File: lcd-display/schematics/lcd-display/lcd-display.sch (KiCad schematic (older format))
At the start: 11 parts, among them U1 74LS00, U2 74LS04, U3 74LS245, U4 74LS32

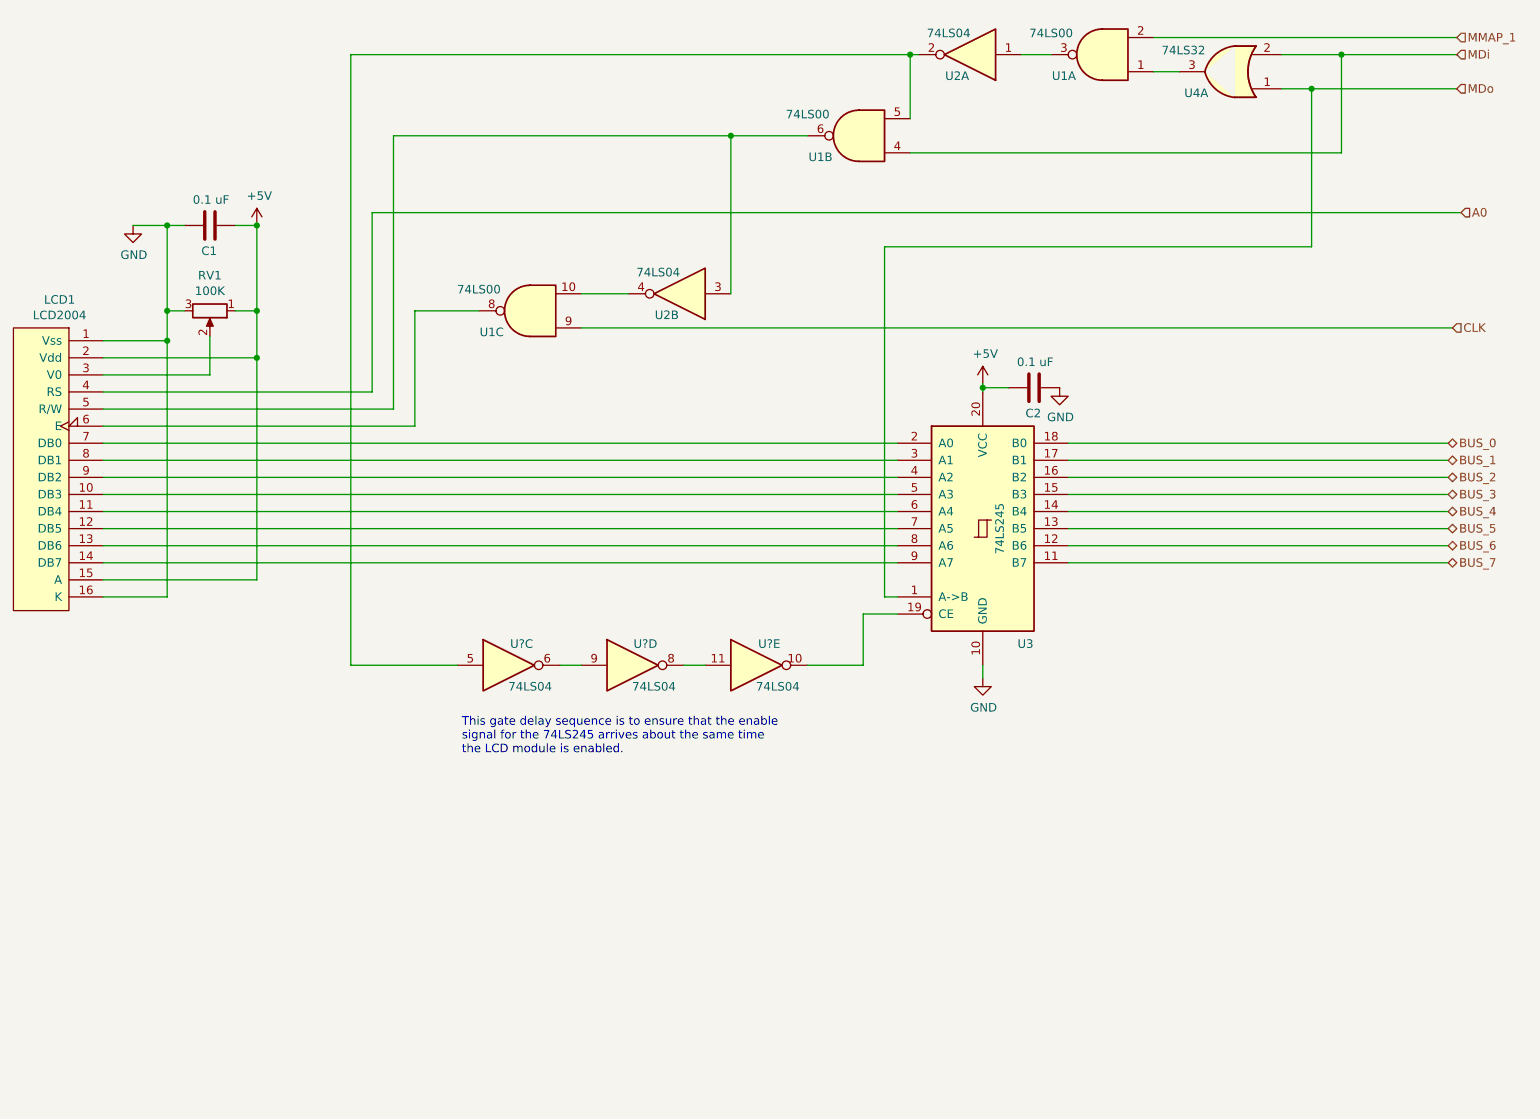
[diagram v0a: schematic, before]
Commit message: first working version of LCD module
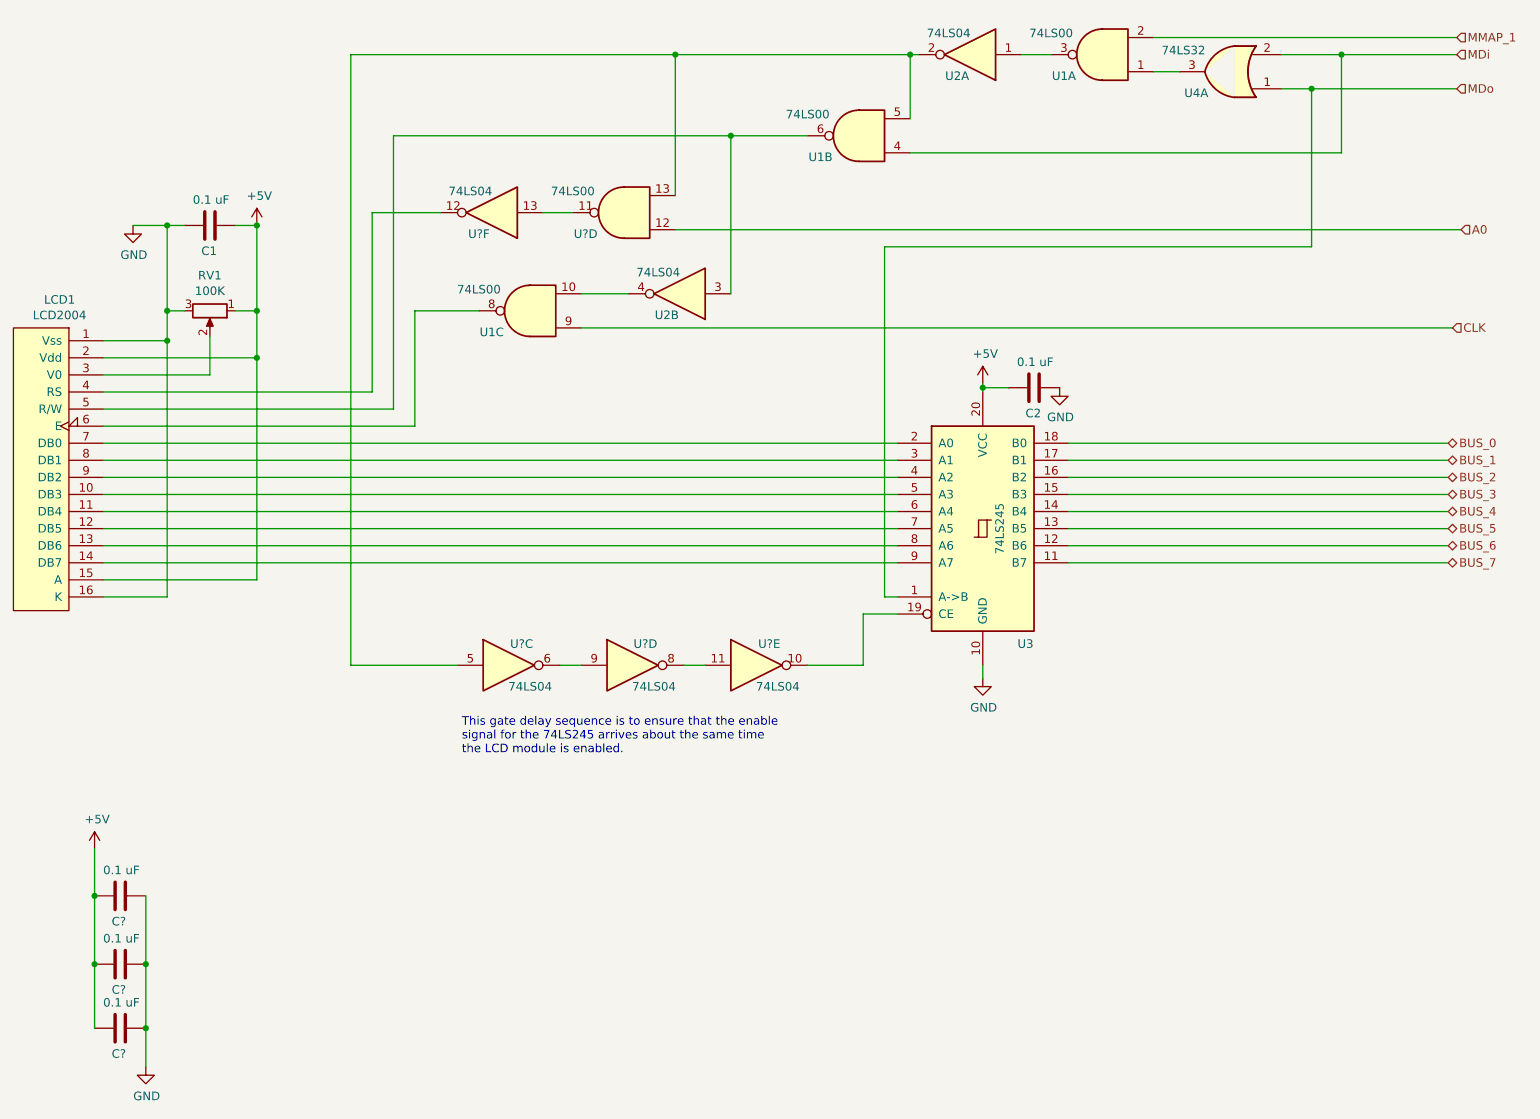
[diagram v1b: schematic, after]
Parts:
- added C? (x3): 0.1 uF, symbol Device:C
- added U?: 74LS00, symbol 74xx:74LS00
- added U?: 74LS04, symbol 74xx:74LS04
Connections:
- net +5V: now also C?.2, C?.2, C?.2
- net A0: now also U?.12; no longer LCD1.4 (RS)
- net GND: now also C?.1, C?.1, C?.1
- net at U1.5, U2.2, U?.5: now also U?.13
- new net: LCD1.4 (RS), U?.12
- new net: U?.11, U?.13
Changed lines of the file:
@@
 Wire Wire Line
 	9250 1475 6725 1475
-Text HLabel 9950 1825 2    50   Input ~ 0
+Text HLabel 9950 1925 2    50   Input ~ 0
 A0
 Text HLabel 9900 2500 2    50   Input ~ 0
@@
 $EndComp
 Wire Wire Line
-	8150 800  9925 800
-Wire Wire Line
 	5675 2300 5675 1375
 Connection ~ 5675 1375
@@
 Wire Wire Line
 	3825 2400 4200 2400
-Wire Wire Line
-	9950 1825 3575 1825
 Wire Wire Line
 	3575 1825 3575 2875
@@
 	4675 4475 4800 4475
 Wire Wire Line
-	6725 900  3450 900
+	6725 900  5350 900
 Wire Wire Line
 	3450 900  3450 4475
@@
 Text Notes 4100 5000 0    50   ~ 0
 This gate delay sequence is to ensure that the enable\nsignal for the 74LS245 arrives about the same time\nthe LCD module is enabled.
+$Comp
+L Device:C C?
+U 1 1 61D87343
+P 2100 5825
+F 0 "C?" V 2250 5775 50  0000 L CNN
+F 1 "0.1 uF" V 1950 5725 50  0000 L CNN
+F 2 "" H 2138 5675 50  0001 C CNN
+F 3 "~" H 2100 5825 50  0001 C CNN
+	1    2100 5825
+	0    1    1    0
+$EndComp
+$Comp
+L Device:C C?
+U 1 1 61D87A90
+P 2100 6225
+F 0 "C?" V 2250 6175 50  0000 L CNN
+F 1 "0.1 uF" V 1950 6125 50  0000 L CNN
+F 2 "" H 2138 6075 50  0001 C CNN
+F 3 "~" H 2100 6225 50  0001 C CNN
+	1    2100 6225
+	0    1    1    0
+$EndComp
+$Comp
+L Device:C C?
+U 1 1 61D8812F
+P 2100 6600
+F 0 "C?" V 2250 6550 50  0000 L CNN
+F 1 "0.1 uF" V 1950 6500 50  0000 L CNN
+F 2 "" H 2138 6450 50  0001 C CNN
+F 3 "~" H 2100 6600 50  0001 C CNN
+	1    2100 6600
+	0    1    1    0
+$EndComp
+Wire Wire Line
+	1950 6600 1950 6225
+Wire Wire Line
+	1950 6225 1950 5825
+Connection ~ 1950 6225
+Wire Wire Line
+	2250 5825 2250 6225
+Wire Wire Line
+	2250 6225 2250 6600
+Connection ~ 2250 6225
+$Comp
+L power:GND #PWR?
+U 1 1 61D90BAC
+P 2250 6825
+F 0 "#PWR?" H 2250 6575 50  0001 C CNN
+F 1 "GND" H 2255 6652 50  0000 C CNN
+F 2 "" H 2250 6825 50  0001 C CNN
+F 3 "" H 2250 6825 50  0001 C CNN
+	1    2250 6825
+	1    0    0    -1
+$EndComp
+$Comp
+L power:+5V #PWR?
+U 1 1 61D91162
+P 1950 5550
+F 0 "#PWR?" H 1950 5400 50  0001 C CNN
+F 1 "+5V" H 1965 5723 50  0000 C CNN
+F 2 "" H 1950 5550 50  0001 C CNN
+F 3 "" H 1950 5550 50  0001 C CNN
+	1    1950 5550
+	1    0    0    -1
+$EndComp
+Wire Wire Line
+	1950 5825 1950 5550
+Connection ~ 1950 5825
+Wire Wire Line
+	2250 6600 2250 6825
+Connection ~ 2250 6600
+$Comp
+L 74xx:74LS00 U?
+U 4 1 61CB2133
+P 5050 1825
+F 0 "U?" H 5275 1950 50  0000 C CNN
+F 1 "74LS00" H 5350 1700 50  0000 C CNN
+F 2 "" H 5050 1825 50  0001 C CNN
+F 3 "http://www.ti.com/lit/gpn/sn74ls00" H 5050 1825 50  0001 C CNN
+	4    5050 1825
+	-1   0    0    1
+$EndComp
+$Comp
+L 74xx:74LS04 U?
+U 6 1 61CBA352
+P 4275 1825
+F 0 "U?" H 4350 1950 50  0000 C CNN
+F 1 "74LS04" H 4400 1700 50  0000 C CNN
+F 2 "" H 4275 1825 50  0001 C CNN
+F 3 "http://www.ti.com/lit/gpn/sn74LS04" H 4275 1825 50  0001 C CNN
+	6    4275 1825
+	-1   0    0    1
+$EndComp
+Wire Wire Line
+	3575 1825 3975 1825
+Wire Wire Line
+	4575 1825 4750 1825
+Wire Wire Line
+	5350 1925 9950 1925
+Wire Wire Line
+	8150 800  9925 800
+Wire Wire Line
+	5350 1725 5350 900
+Connection ~ 5350 900
+Wire Wire Line
+	5350 900  3450 900
 $EndSCHEMATC

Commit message: improved handling of timming differences between clock and mmap
The MMAP_1 signal is noticablylater than the clock due to all the gates it has to go through in the memory map mananger. This caused issues with the trailing edge enable fo the LCD2004 module in that the inverted clock would go high moments before the MMAP_1 signal would go low. This in turn caused a spurious trailing edge event into the Enable input of the LCD2004 module, causing weirdness with the cursor.
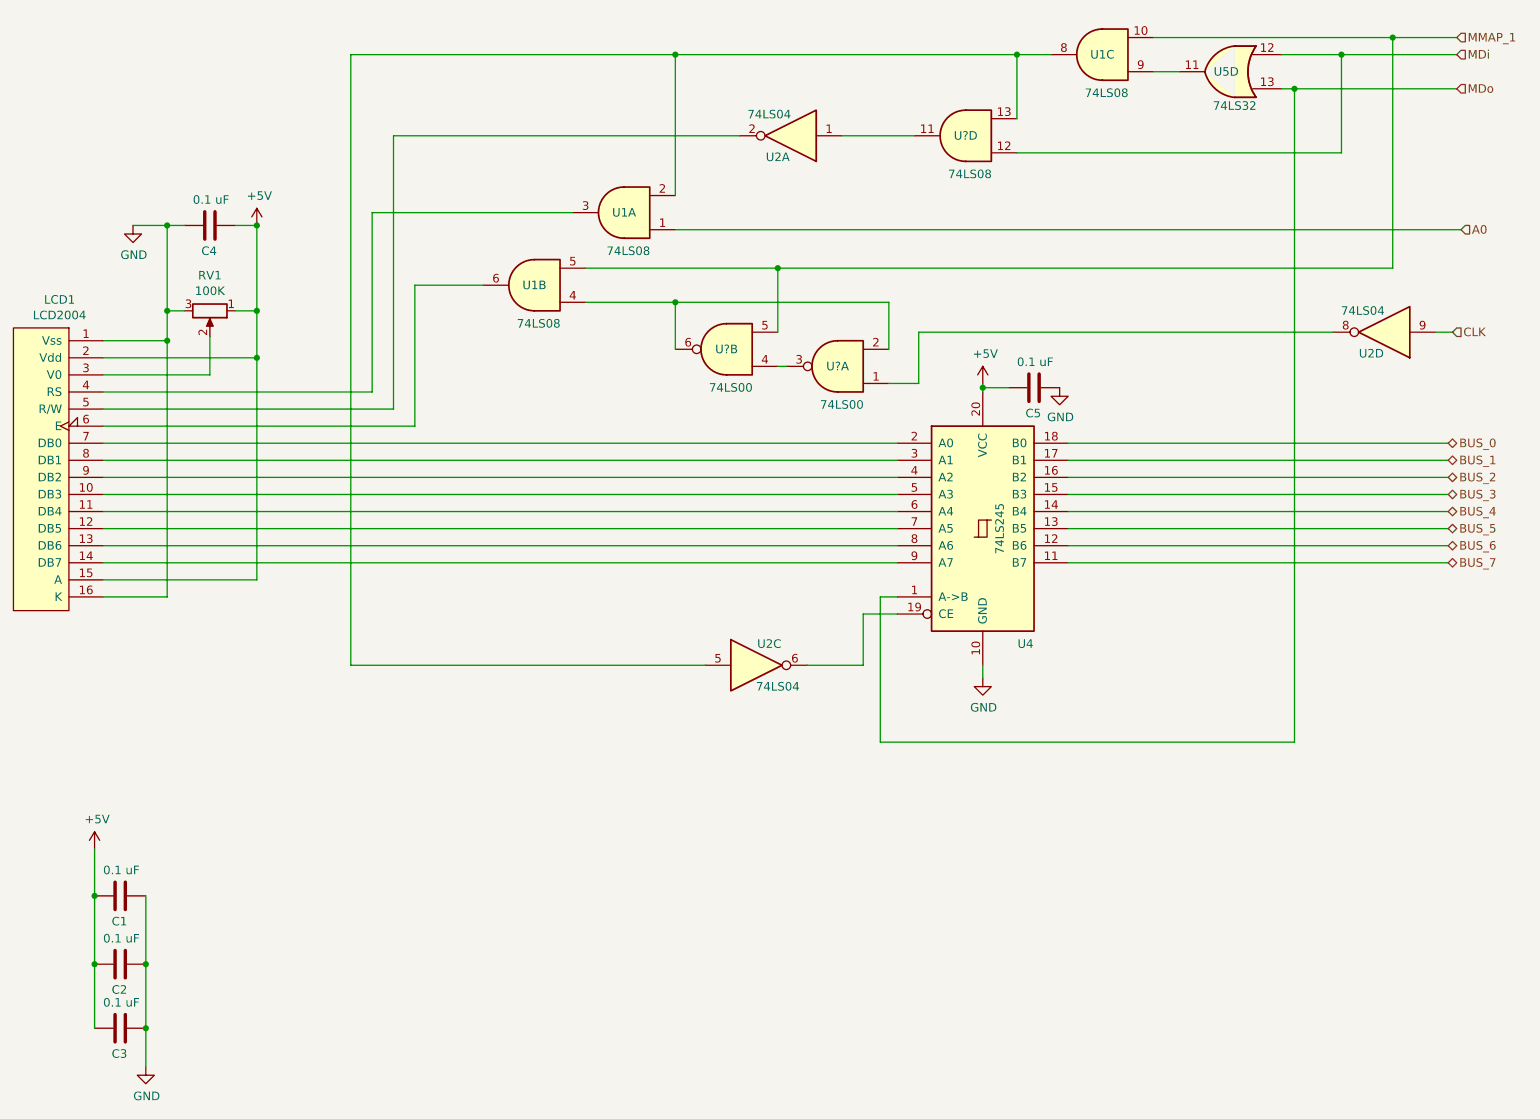
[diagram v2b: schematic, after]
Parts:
- removed U1, U?: 74LS00, symbol 74xx:74LS00
- removed U2, U?: 74LS04, symbol 74xx:74LS04
- added U1, U?: 74LS08, symbol 74xx:74LS08
- added U? (x2): 74LS00, symbol 74xx:74LS00
- gave numbers to parts that had none: 4
- renumbered C1 to C4, C2 to C5, U3 to U4, U4 to U5
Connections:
- net A0: now also U1.1
- net CLK: now also U2.9
- net MDi: now also U5.12, U?.12; no longer U5.2
- net MDo: now also U5.13; no longer U5.1
- net MMAP_1: now also U1.10, U1.5, U?.5
- net at LCD1.4 (RS): now also U1.3
- net at LCD1.5 (R/W): now also U2.2
- net at LCD1.6 (E): now also U1.6
- net at U4.19 (CE): now also U2.6; no longer U2.10
- net at U2.8: now also U?.1; no longer U2.11
- new net: U1.9, U5.11
- new net: U1.2, U1.8, U2.5, U?.13
- new net: U1.4, U?.2, U?.6
- new net: U2.1, U?.11
- new net: U?.3, U?.4
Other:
- note removed: "This gate delay sequence is to ensure that the enable\nsignal for the 74LS245 arrives about the same time\nthe LCD module is enabled."
- moved on the sheet: U2D

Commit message: address stability issues caused by inductance
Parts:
- removed unit 2 of U1
- added C6: 1 pF, symbol Device:C
- added unit 3 of U1
- gave numbers to parts that had none: 2
- renumbered U1 to U2, U2 to U3
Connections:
- net GND: now also C6.2
- net MDi: now also C6.1
- net MMAP_1: no longer U1.5
- net at LCD1.6 (E): now also U1.8
- net at U2.11, U3.1: now also U1.5, U1.10
- net at U1.3, U1.4: now also U1.9
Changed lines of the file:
@@
 $EndComp
 Wire Wire Line
-	9925 900  9250 900
+	9925 900  9650 900
 Wire Wire Line
 	8300 1000 8150 1000
@@
 	2000 2775 2625 2775
 $Comp
-L 74xx:74LS04 U2
+L 74xx:74LS04 U3
 U 3 1 61D71BDF
 P 5825 4475
-F 0 "U2" H 5900 4600 50  0000 C CNN
+F 0 "U3" H 5900 4600 50  0000 C CNN
 F 1 "74LS04" H 5950 4350 50  0000 C CNN
 F 2 "" H 5825 4475 50  0001 C CNN
@@
 $EndComp
 $Comp
-L 74xx:74LS04 U2
+L 74xx:74LS04 U3
 U 4 1 61D73754
 P 9500 2525
-F 0 "U2" H 9575 2650 50  0000 C CNN
+F 0 "U3" H 9575 2650 50  0000 C CNN
 F 1 "74LS04" H 9625 2400 50  0000 C CNN
 F 2 "" H 9500 2525 50  0001 C CNN
@@
 $EndComp
 $Comp
-L 74xx:74LS04 U2
+L 74xx:74LS04 U3
 U 1 1 61D74674
 P 6025 1375
-F 0 "U2" H 6100 1500 50  0000 C CNN
+F 0 "U3" H 6100 1500 50  0000 C CNN
 F 1 "74LS04" H 6150 1250 50  0000 C CNN
 F 2 "" H 6025 1375 50  0001 C CNN
@@
 	5350 1925 9950 1925
 Wire Wire Line
-	8150 800  9550 800
-Wire Wire Line
 	5350 1725 5350 900
 Connection ~ 5350 900
@@
 	5350 900  3450 900
 $Comp
-L 74xx:74LS08 U1
+L 74xx:74LS08 U2
 U 3 1 61D13CBF
 P 7850 900
-F 0 "U1" H 7850 900 50  0000 C CNN
+F 0 "U2" H 7850 900 50  0000 C CNN
 F 1 "74LS08" H 7825 1125 50  0000 C CNN
 F 2 "" H 7850 900 50  0001 C CNN
@@
 	7350 900  7550 900
 $Comp
-L 74xx:74LS08 U1
+L 74xx:74LS08 U2
 U 1 1 61D21297
 P 5050 1825
-F 0 "U1" H 5050 1825 50  0000 C CNN
+F 0 "U2" H 5050 1825 50  0000 C CNN
 F 1 "74LS08" H 5025 2050 50  0000 C CNN
 F 2 "" H 5050 1825 50  0001 C CNN
@@
 Wire Wire Line
 	3700 1375 5725 1375
-$Comp
-L 74xx:74LS08 U1
-U 2 1 61D5EE45
-P 4525 2250
-F 0 "U1" H 4525 2250 50  0000 C CNN
-F 1 "74LS08" H 4500 2475 50  0000 C CNN
-F 2 "" H 4525 2250 50  0001 C CNN
-F 3 "http://www.ti.com/lit/gpn/sn74LS08" H 4525 2250 50  0001 C CNN
-	2    4525 2250
-	-1   0    0    1
-$EndComp
 Wire Wire Line
 	3450 4475 5525 4475
@@
 	3825 2250 3825 3075
 $Comp
-L 74xx:74LS08 U?
+L 74xx:74LS08 U2
 U 4 1 61DA5054
 P 7050 1375
-F 0 "U?" H 7050 1375 50  0000 C CNN
+F 0 "U2" H 7050 1375 50  0000 C CNN
 F 1 "74LS08" H 7025 1600 50  0000 C CNN
 F 2 "" H 7050 1375 50  0001 C CNN
@@
 	9800 2525 9900 2525
 $Comp
-L 74xx:74LS00 U?
+L 74xx:74LS00 U1
 U 1 1 61DBB399
 P 6300 2725
-F 0 "U?" H 6300 2725 50  0000 C CNN
+F 0 "U1" H 6300 2725 50  0000 C CNN
 F 1 "74LS00" H 6275 2950 50  0000 C CNN
 F 2 "" H 6300 2725 50  0001 C CNN
@@
 $EndComp
 $Comp
-L 74xx:74LS00 U?
+L 74xx:74LS00 U1
 U 2 1 61DC0804
 P 5650 2625
-F 0 "U?" H 5650 2625 50  0000 C CNN
+F 0 "U1" H 5650 2625 50  0000 C CNN
 F 1 "74LS00" H 5625 2850 50  0000 C CNN
 F 2 "" H 5650 2625 50  0001 C CNN
@@
 $EndComp
 Wire Wire Line
-	4825 2350 5350 2350
-Wire Wire Line
 	6600 2350 6600 2625
 Wire Wire Line
@@
 Wire Wire Line
 	5350 2625 5350 2350
-Connection ~ 5350 2350
 Wire Wire Line
 	5350 2350 6600 2350
@@
 Wire Wire Line
 	5350 900  7350 900
+Wire Wire Line
+	6325 1375 6500 1375
+Wire Wire Line
+	8150 800  9925 800
+Wire Wire Line
+	5950 2150 6500 2150
+Wire Wire Line
+	6500 2150 6500 1375
 Connection ~ 5950 2150
-Wire Wire Line
-	6325 1375 6750 1375
-Wire Wire Line
-	9550 2150 9550 800
-Wire Wire Line
-	5950 2150 9550 2150
-Connection ~ 9550 800
-Wire Wire Line
-	9550 800  9925 800
+Connection ~ 6500 1375
+Wire Wire Line
+	6500 1375 6750 1375
+Wire Wire Line
+	6000 2725 6000 2975
+Wire Wire Line
+	6000 2975 4825 2975
+Wire Wire Line
+	4825 2975 4825 2350
+Connection ~ 6000 2725
+$Comp
+L 74xx:74LS00 U1
+U 3 1 61D07816
+P 4525 2250
+F 0 "U1" H 4525 2250 50  0000 C CNN
+F 1 "74LS00" H 4500 2475 50  0000 C CNN
+F 2 "" H 4525 2250 50  0001 C CNN
+F 3 "http://www.ti.com/lit/gpn/sn74ls00" H 4525 2250 50  0001 C CNN
+	3    4525 2250
+	-1   0    0    1
+$EndComp
+$Comp
+L Device:C C6
+U 1 1 61D0EEB6
+P 9650 1400
+F 0 "C6" H 9765 1446 50  0000 L CNN
+F 1 "1 pF" H 9765 1355 50  0000 L CNN
+F 2 "" H 9688 1250 50  0001 C CNN
+F 3 "~" H 9650 1400 50  0001 C CNN
+	1    9650 1400
+	1    0    0    -1
+$EndComp
+$Comp
+L power:GND #PWR08
+U 1 1 61D0FAEC
+P 9650 1550
+F 0 "#PWR08" H 9650 1300 50  0001 C CNN
+F 1 "GND" H 9655 1377 50  0000 C CNN
+F 2 "" H 9650 1550 50  0001 C CNN
+F 3 "" H 9650 1550 50  0001 C CNN
+	1    9650 1550
+	1    0    0    -1
+$EndComp
+Wire Wire Line
+	9650 1250 9650 900
+Connection ~ 9650 900
+Wire Wire Line
+	9650 900  9250 900
 $EndSCHEMATC

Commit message: updated LCD module schematic
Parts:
- removed U1: 74LS00, symbol 74xx:74LS00
- removed unit 1 of U3
- added unit 3 of U1
- added unit 2 of U1
- added unit 1 of U1
- added unit 2 of U2
- renumbered U3 to U1, U4 to U3, U5 to U4
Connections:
- net A0: now also U2.13; no longer U2.1
- net CLK: now also U1.11; no longer U1.9
- net MDi: now also U2.1; no longer U2.12
- net MMAP_1: now also U2.12, U2.2
- net at LCD1.4 (RS): now also U2.11; no longer U2.3
- net at LCD1.5 (R/W): now also U1.6
- net at LCD1.6 (E): now also U1.2
- net at U3.19 (CE): now also U1.8; no longer U1.6
- new net: U1.9, U2.5, U2.8
- new net: U1.10, U2.4
- new net: U1.5, U2.3
- new net: U1.3, U2.6
- new net: U1.1, U1.4
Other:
- note added: "These double inverters are to ensure the\nclock signal arives after the LCD module \nhas responsed to the RS and R/W signals."
- moved on the sheet: C6, U2C, U4D
